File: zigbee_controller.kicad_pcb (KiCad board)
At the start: 2 copper layers, 55 x 65 mm, 79 parts, among them J1 KF635, J10 TerminalBlock_KF301-5.0, J11 TerminalBlock_KF301-5.0, J12 TerminalBlock_KF301-5.0, J13 TerminalBlock_KF301-5.0, J3 Conn_01x06, J4 Conn_01x07, J5 Conn_01x05, P1 USB_C_Receptacle_GCT_USB4105, Q2 IRLB3813, Q3 IRLB3813, Q4 IRLB3813, Q5 IRLB3813, SW2 EN, SW4 Boot, U1 TPS54560, U2 ESP32-C6-MINI-1, U4 TC4427, U5 TC4427, U6 RT9080, U9 CH224K

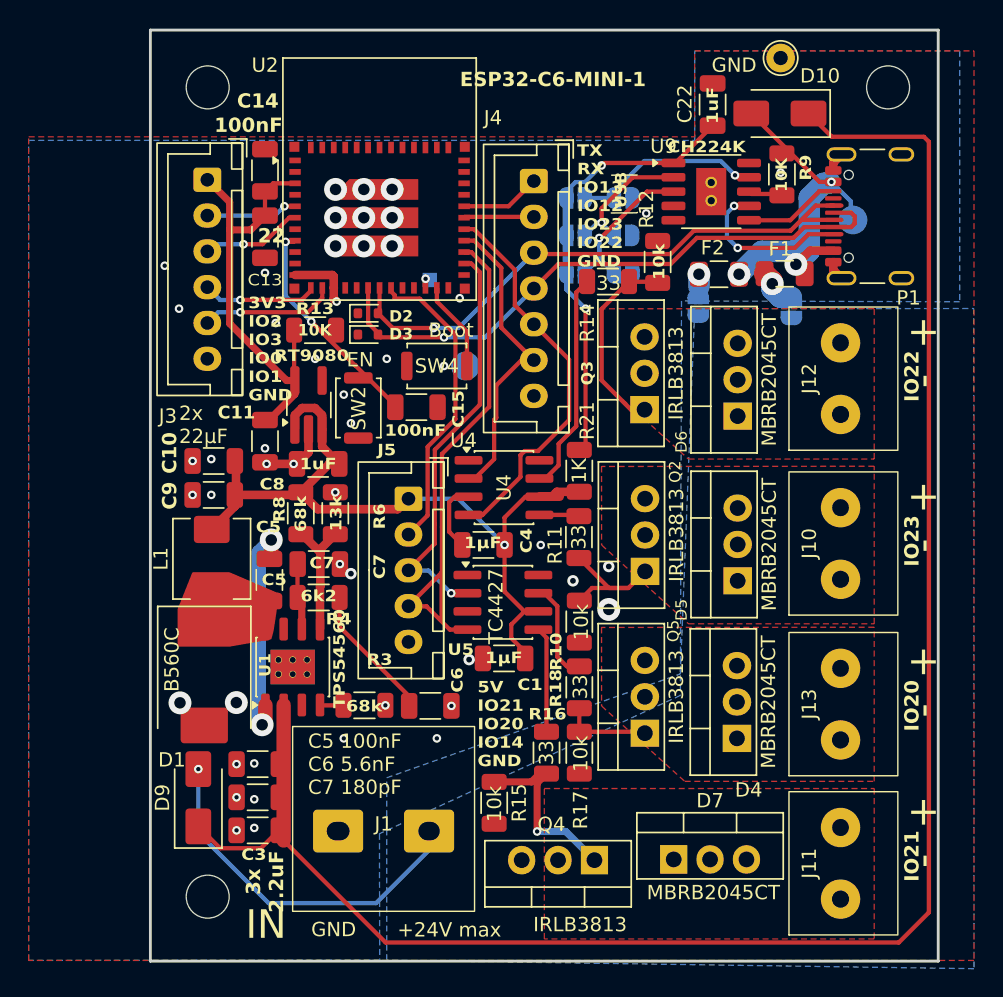
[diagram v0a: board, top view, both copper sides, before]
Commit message: Double pads for USB power
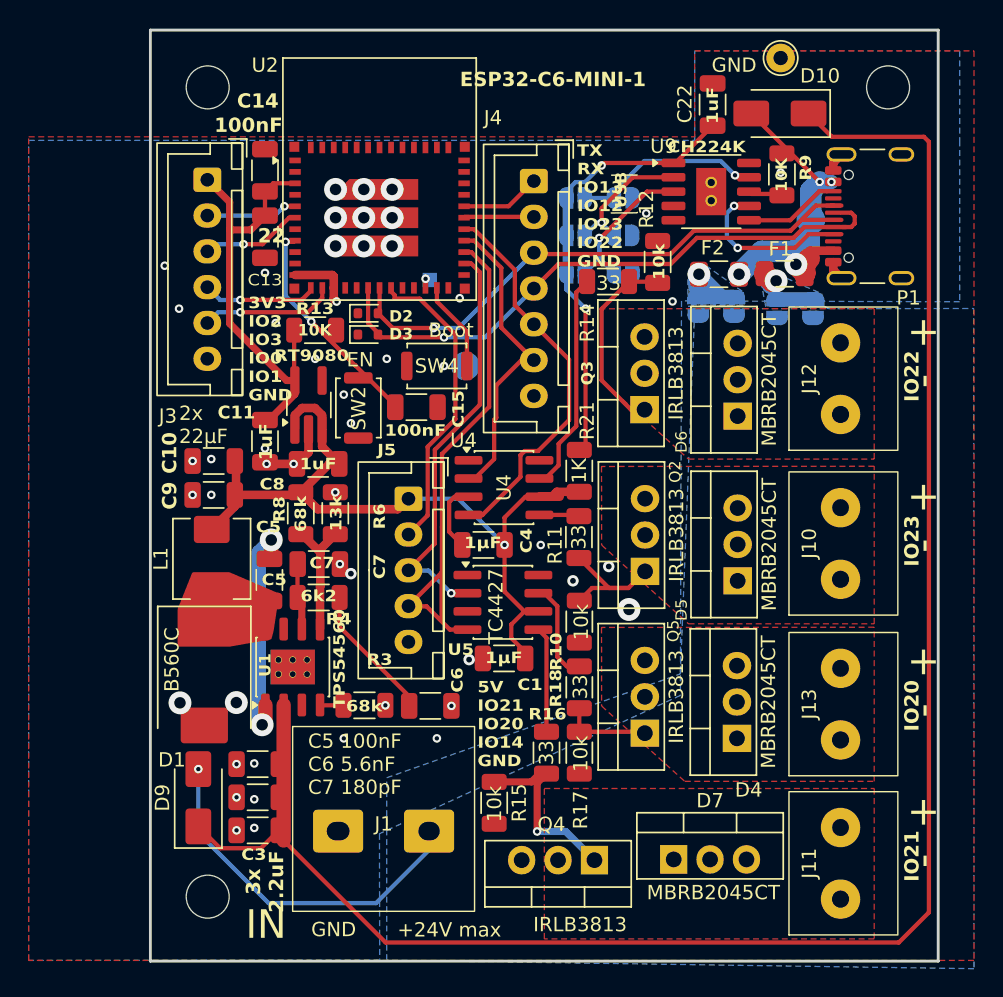
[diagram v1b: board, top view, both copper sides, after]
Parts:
- added JP11: USB power 3A, Jumper:SolderJumper-2_P1.3mm_Open_RoundedPad1.0x1.5mm, B.Cu at (193.2, 87.8)
- added JP8: USB power 5A, Jumper:SolderJumper-2_P1.3mm_Open_RoundedPad1.0x1.5mm, B.Cu at (198.8, 87.9)
- moved TP4 2.94 mm to (198.6, 81.8)
- moved JP7 1.00 mm to (196.2, 88.0)
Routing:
- net Net-(JP10-B): track 0.92 -> 6.53 mm
- net VBUS: track 27.5 -> 25.7 mm, vias 3 -> 4
- net Net-(JP7-B): track 3.27 -> 3.91 mm
- net GND: vias 49 -> 50
- added copper zone on B.Cu, net Net-(JP10-B)
- added copper zone on B.Cu, net Net-(JP7-B)
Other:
- board text added: "- 2oz copper - U1: TPS54560 - U4/U5: TC4427 - U6: RT9080 - U9: CH224K - D1: B650C - J1: KF635 - Q2-Q5: IRLB3813 - SW1/SW2: 3x4x2 switch - L1: 1040 10μH inductor 0530 - J10-J13: KF301-5.0 - D4-D7: Optional fly-back diode MBRB2045CT (Schottky) - D2/D3: LESD5D5.0CT1G"
- board text added: "|V |CFG1|CFG2|CFG3| |---|----|----|----| |5V | 1 | 0 | 0 | |9V | 0 | 0 | 0 | |12V| 0 | 0 | 1 | |15V| 0 | 1 | 1 | |20V| 0 | 1 | 0 |"
- board text removed: "- 2oz copper - U1: TPS54560 - U4/U5: TC4427 - U6: RT9080 - U9: CH224K - D1: B650C - J1: KF635 - Q2-Q5: IRLB3813 - SW1/SW2: 3x4x2 switch - L1: 1040 10μH inductor 0530 - J10-J13: KF301-5.0 - D4-D7: Optional fly-back diode MBRB2045CT (Schottky) - D2/D3 LESD5D5.0CT1G"
- board text removed: "|V |CFG1|CFG2|CFG3| |---|----|----|----| |5V | 1 | 0 | 0 | |9V | 0 | 0 | 0 | |12V| 0 | 0 | 1 | |15V| 0 | 1 | 1 | |20V| 0 | 1 | 0"

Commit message: Optimize VBUS vias
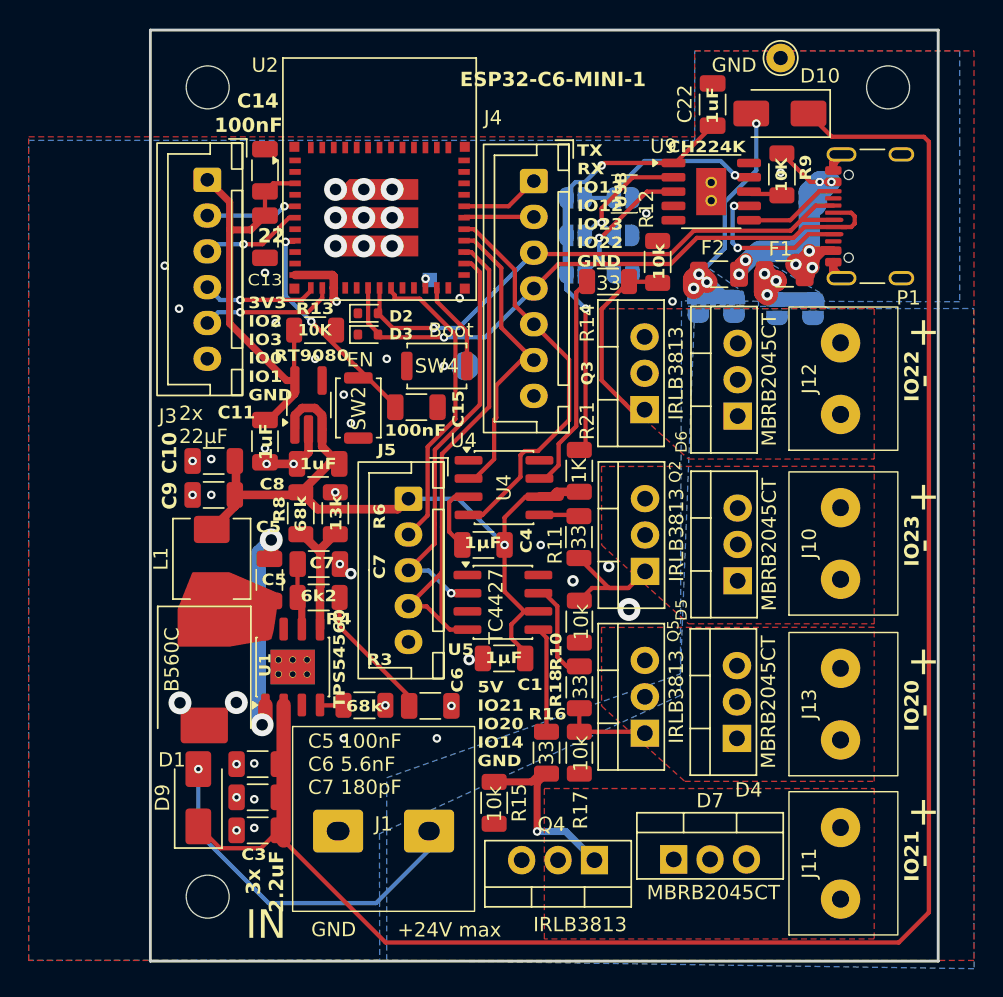
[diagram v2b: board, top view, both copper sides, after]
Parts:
- moved TP4 1.22 mm to (198.8, 80.5)
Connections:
- net Net-(JP7-B) renamed /fused_VBUS_5A
- D10 pad 2: VBUS -> fused_VBUS_3A
- F2 pad 2: Net-(JP10-B) -> fused_VBUS_3A
- JP10 pad 2: Net-(JP10-B) -> fused_VBUS_3A
- JP11 pad 2: Net-(JP10-B) -> fused_VBUS_3A
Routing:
- net fused_VBUS_3A: track 0.00 -> 19.0 mm, vias 0 -> 4
- net VBUS: track 25.7 -> 34.0 mm, vias 4 -> 7
- net Net-(JP10-B): track 6.53 -> 0.00 mm, vias 1 -> 0
- net +24V: track 25.4 -> 24.1 mm
- net /fused_VBUS_5A: track 3.91 -> 5.09 mm, vias 1 -> 3
- net /IO13-usb: track 41.0 -> 40.2 mm
- added copper zone on B.Cu, net fused_VBUS_3A
- removed copper zone on B.Cu, net Net-(JP10-B)

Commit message: Add ground testing point
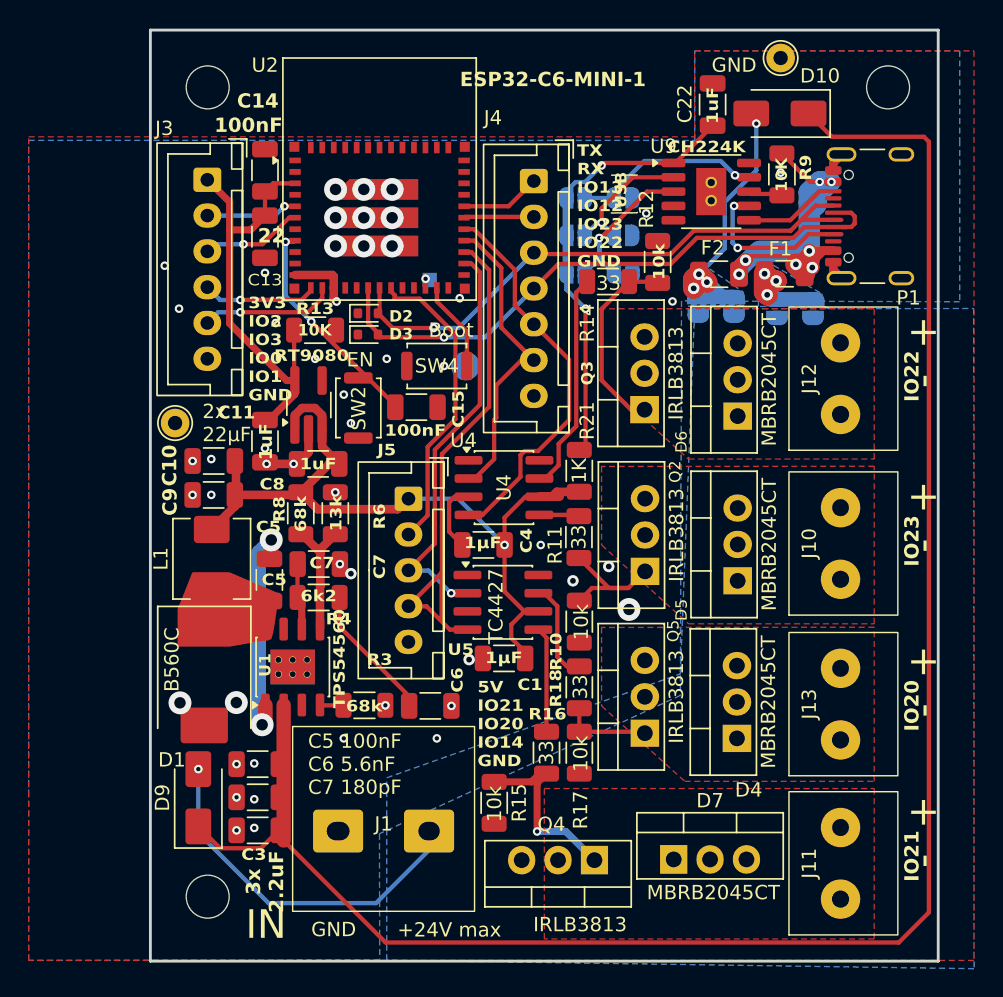
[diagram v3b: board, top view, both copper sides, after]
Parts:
- added TP6: GND, TestPoint:TestPoint_THTPad_D2.0mm_Drill1.0mm, F.Cu at (154.2, 95.9)
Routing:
- net VBUS: track 34.0 -> 39.3 mm

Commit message: Add pulldown resistors between ESP32 and TC4427
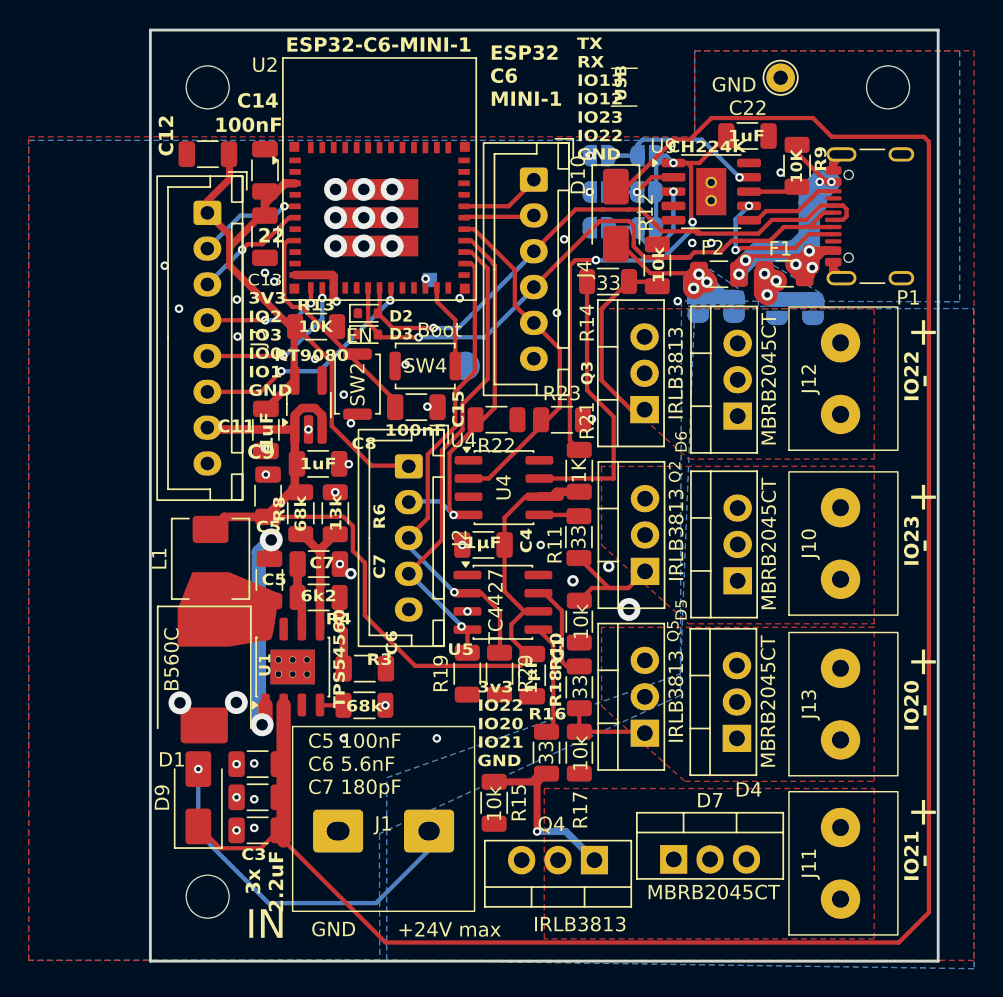
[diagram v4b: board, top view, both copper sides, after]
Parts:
- removed C10: 22μF, Capacitor_SMD:C_1206_3216Metric
- removed J5: Conn_01x05, Connector_JST:JST_XH_B5B-XH-A_1x05_P2.50mm_Vertical
- removed TP6: GND, TestPoint:TestPoint_THTPad_D2.0mm_Drill1.0mm
- added C12: 1uF, Capacitor_SMD:C_1206_3216Metric, F.Cu at (156.5, 77.2)
- added J2: Conn_01x05, Connector_JST:JST_XH_B5B-XH-A_1x05_P2.50mm_Vertical, F.Cu at (170.5, 99.0)
- added R19: 10k, Resistor_SMD:R_1206_3216Metric, F.Cu at (174.6, 113.4)
- added R20: 10k, Resistor_SMD:R_1206_3216Metric, F.Cu at (176.9, 113.4)
- added R22: 10k, Resistor_SMD:R_1206_3216Metric, F.Cu at (176.7, 95.7)
- added R23: 10k, Resistor_SMD:R_1206_3216Metric, F.Cu at (181.2, 95.7)
- C9: value 22μF -> 47μF
- J3: value Conn_01x06 -> Conn_01x08; footprint Connector_JST:JST_XH_B6B-XH-A_1x06_P2.50mm_Vertical -> Connector_JST:JST_XH_B8B-XH-A_1x08_P2.50mm_Vertical
- J4: value Conn_01x07 -> Conn_01x06; footprint Connector_JST:JST_XH_B7B-XH-A_1x07_P2.50mm_Vertical -> Connector_JST:JST_XH_B6B-XH-A_1x06_P2.50mm_Vertical
- moved D10 13.5 mm to (185.0, 81.4), turned to -90 degrees
- moved JP4 5.88 mm to (187.2, 82.3), turned to 0 degrees
- moved JP5 5.80 mm to (187.1, 79.8), turned to 0 degrees
- moved JP6 5.78 mm to (187.2, 77.3), turned to 0 degrees
- moved C6 5.26 mm to (167.5, 113.1)
- moved C9 3.80 mm to (160.7, 101.0), turned to 90 degrees
- moved JP1 3.58 mm to (183.8, 82.3), turned to 180 degrees
- moved JP2 3.45 mm to (183.8, 79.8), turned to 180 degrees
- moved JP3 3.40 mm to (183.8, 77.3), turned to 180 degrees
- moved C22 3.27 mm to (194.2, 75.9), turned to 0 degrees
- moved J3 2.31 mm to (156.5, 81.3)
- moved C1 2.29 mm to (179.2, 113.5), turned to -90 degrees
- moved SW2 1.67 mm to (167.0, 93.2)
- moved TP3 1.38 mm to (196.5, 71.8)
- moved R9 1.21 mm to (197.6, 78.0)
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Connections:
- J3 pad 6: GND -> /IO14
- J4 pad 6: /IO22 -> GND
- U4 pad 2: /IO22 -> /IO23
- U4 pad 4: /IO23 -> /IO22
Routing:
- net Net-(D10-K): track 128.0 -> 143.4 mm
- net +5V: track 55.8 -> 70.1 mm, vias 1 -> 0
- net 3V3: track 30.6 -> 42.7 mm
- net GND: track 17.1 -> 7.29 mm, vias 50 -> 55
- net /CH224k_Vdd: track 29.6 -> 38.4 mm, vias 2 -> 3
- net /IO22: track 21.2 -> 27.3 mm, vias 0 -> 1
- net fused_VBUS_3A: track 19.0 -> 13.0 mm, vias 4 -> 3
- net /IO12-usb: track 42.0 -> 47.1 mm
- net /IO14: track 21.2 -> 16.3 mm, vias 0 -> 2
- net Net-(U4-OUT_A): track 15.0 -> 19.7 mm
- net Net-(JP2-A): track 9.68 -> 4.96 mm
- net Net-(JP1-A): track 12.2 -> 7.93 mm
- net Net-(C6-Pad1): track 8.92 -> 5.09 mm
- net /IO21: track 36.2 -> 32.5 mm, vias 0 -> 1
- net /IO23: track 27.4 -> 24.0 mm
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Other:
- board text added: "3v3 IO22 IO20 IO21 GND"
- board text added: "ESP32 C6 MINI-1"
- board text removed: "2x 22μF"
- board text removed: "5V IO21 IO20 IO14 GND"

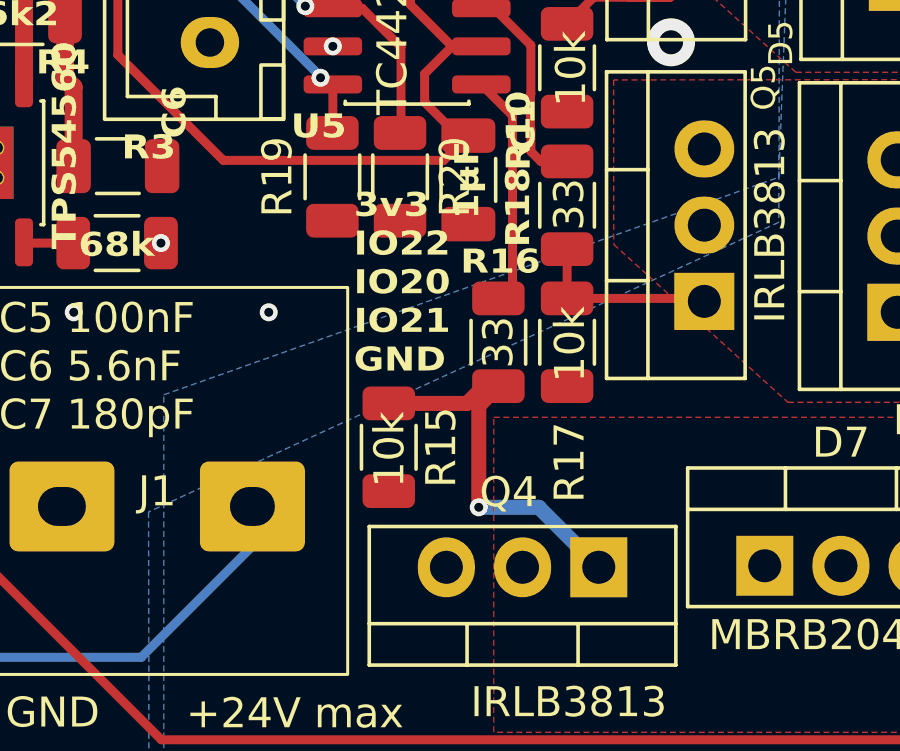
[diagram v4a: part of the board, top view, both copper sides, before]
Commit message: Move J5 textboox and resistor
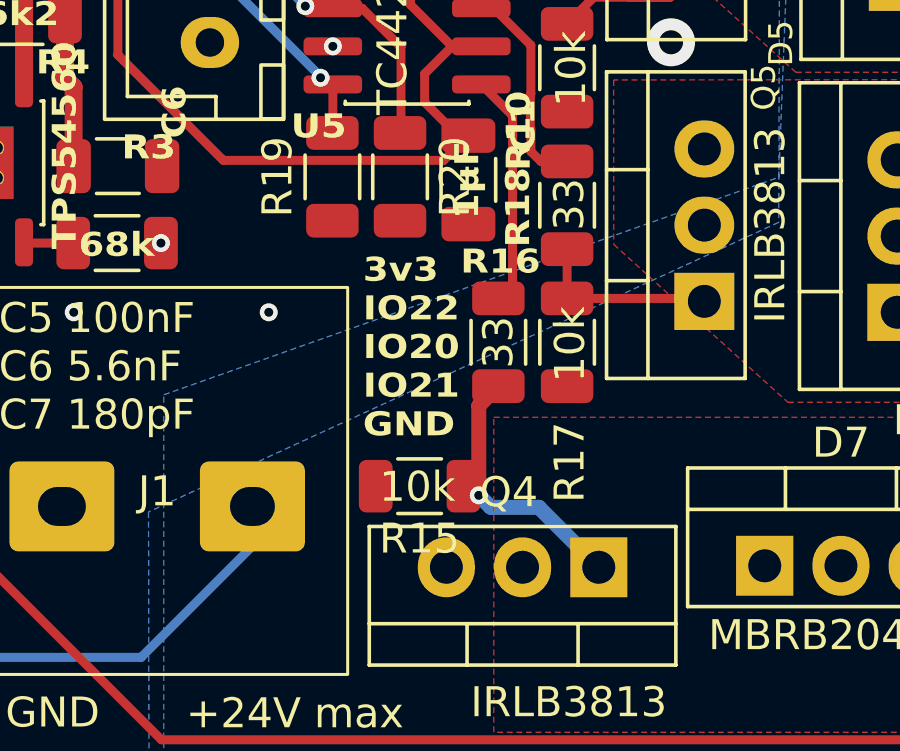
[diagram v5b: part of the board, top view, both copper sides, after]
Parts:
- moved R15 1.66 mm to (177.5, 123.7), turned to 0 degrees
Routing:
- net Net-(Q4-G): track 12.6 -> 8.90 mm

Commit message: Reposition voltage pads text
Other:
- board text added: "- 2oz copper - U1: TPS54560 - U2: ESP32-C6-Mini-1 - U4/U5: TC4427 - U6: RT9080 - U9: CH224K - D1: B650C - J1: KF635 - Q2-Q5: IRLB3813 - SW1/SW2: 3x4x2 switch - L1: 1040 10μH inductor 0530 - J10-J13: KF301-5.0 - D4-D7: Optional fly-back diode MBRB2045CT (Schottky) - D2/D3: LESD5D5.0CT1G"
- board text removed: "- 2oz copper - U1: TPS54560 - U4/U5: TC4427 - U6: RT9080 - U9: CH224K - D1: B650C - J1: KF635 - Q2-Q5: IRLB3813 - SW1/SW2: 3x4x2 switch - L1: 1040 10μH inductor 0530 - J10-J13: KF301-5.0 - D4-D7: Optional fly-back diode MBRB2045CT (Schottky) - D2/D3: LESD5D5.0CT1G"

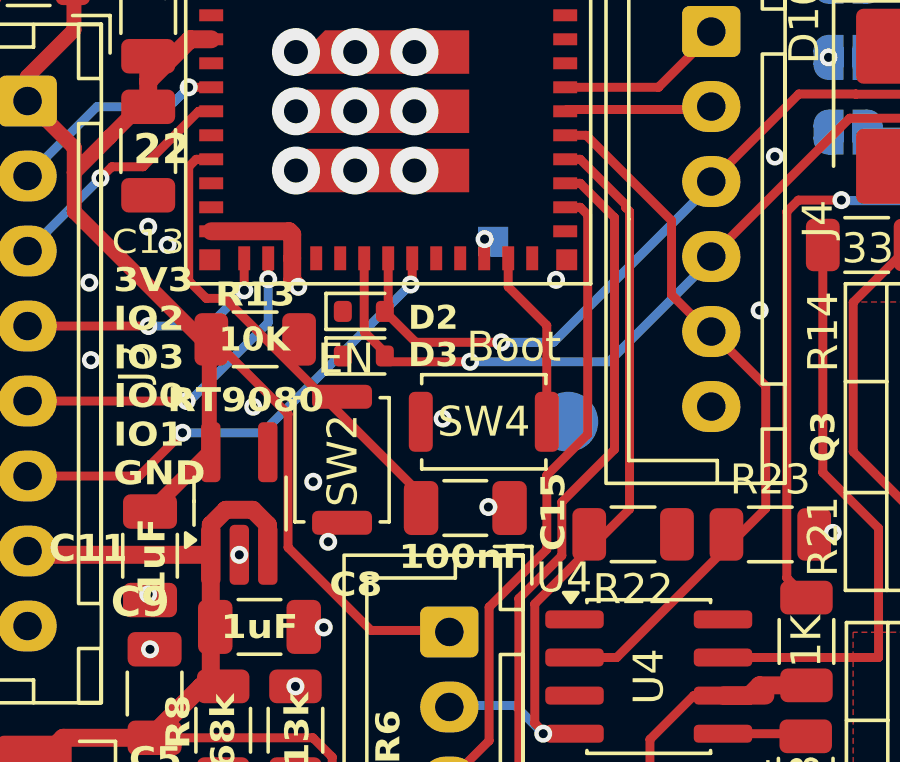
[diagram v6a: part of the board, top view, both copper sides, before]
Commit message: Add extra capacitor to avoid brownout
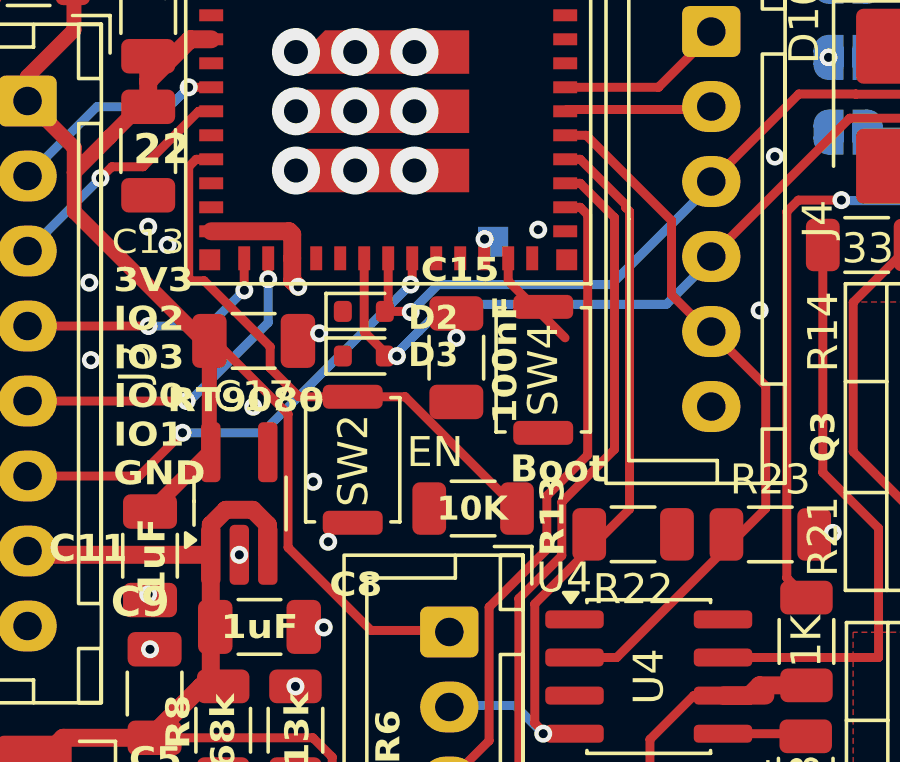
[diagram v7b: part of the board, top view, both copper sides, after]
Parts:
- removed TP5: GND, TestPoint:TestPoint_Pad_D2.0mm
- added C17: 47μF, Capacitor_SMD:C_1206_3216Metric, F.Cu at (164.0, 89.3)
- C13: value 22μF -> 47μF
- moved R13 9.20 mm to (171.3, 94.8)
- moved C15 5.02 mm to (170.8, 89.8), turned to -90 degrees
- moved SW4 2.63 mm to (173.7, 90.2), turned to 90 degrees
- moved SW2 0.36 mm to (167.3, 93.2)
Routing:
- net Net-(U2-EN): track 15.4 -> 19.2 mm
- net Net-(U2-IO9): track 5.17 -> 3.44 mm
- net /IO13-usb: track 41.7 -> 41.0 mm
